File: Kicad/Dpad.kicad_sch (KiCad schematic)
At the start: 12 parts

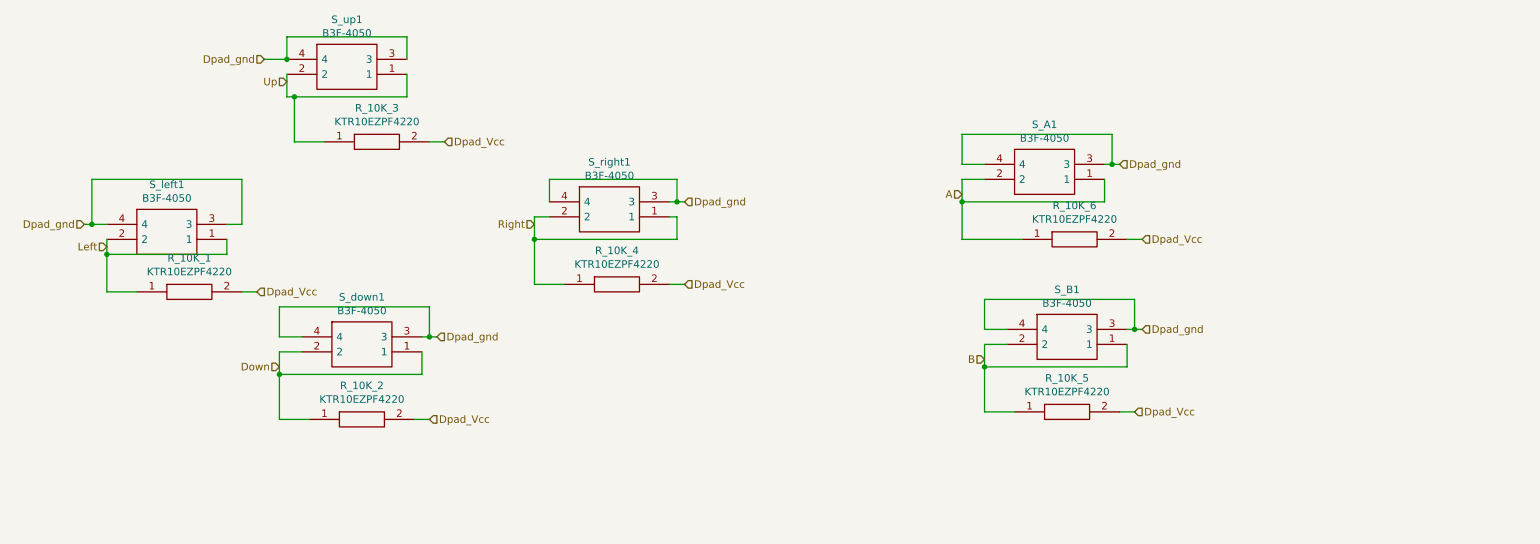
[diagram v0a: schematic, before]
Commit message: New V1.2 Hardware Release
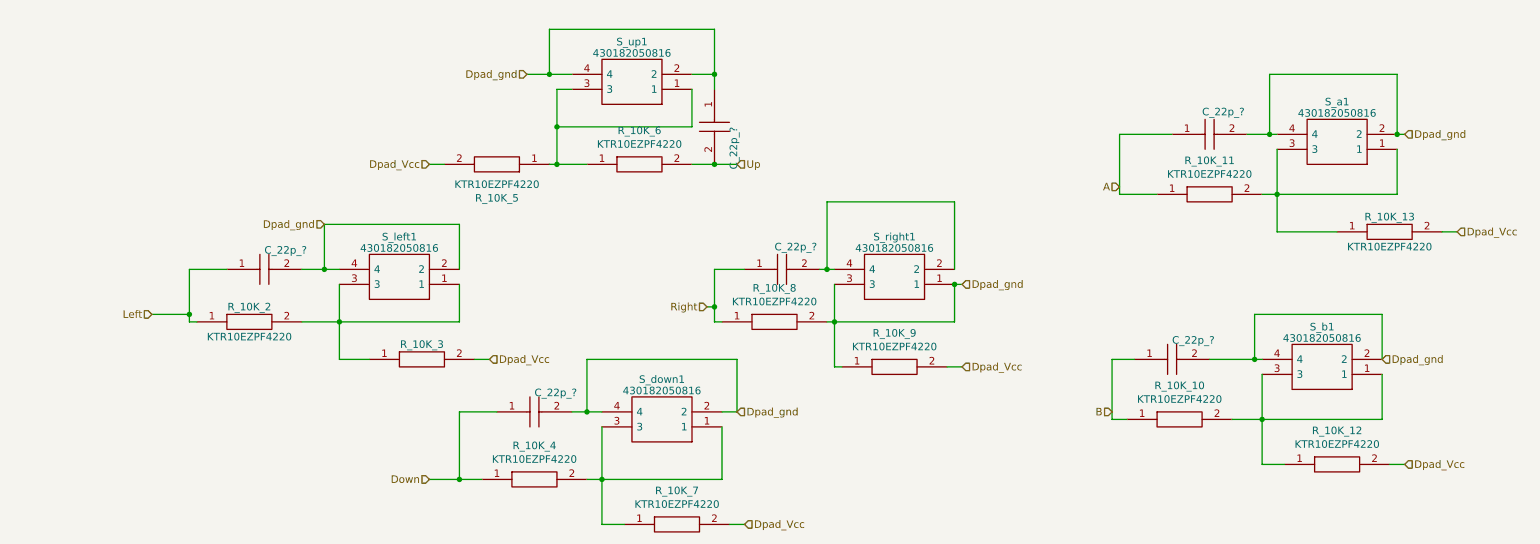
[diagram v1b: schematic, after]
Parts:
- removed S_A1, S_B1, S_down1, S_left1, S_right1, S_up1: B3F-4050, B3F-4000, symbol PicBytesMicro-rescue:B3F-4050-SamacSys_Parts
- added C_22p_? (x6): GCG21BR71H154KA01K, User_lib:CAPC2012X140N, symbol PicBytesMicro-rescue:GCG21BR71H154KA01K-SamacSys_Parts
- added R_10K_10, R_10K_11, R_10K_2, R_10K_4, R_10K_5, R_10K_8: KTR10EZPF4220, User_lib:RESC2012X75N, symbol PicBytesMicro-rescue:KTR10EZPF4220-SamacSys_Parts
- added S_a1, S_b1, S_down1, S_left1, S_right1, S_up1: 430182050816, 430182070816, symbol User_lib:430182050816
- renumbered R_10K_5 to R_10K_12, R_10K_6 to R_10K_13, R_10K_1 to R_10K_3, R_10K_3 to R_10K_6, R_10K_2 to R_10K_7, R_10K_4 to R_10K_9
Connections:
- net A: now also C_22p_?.1, R_10K_11.1; no longer R_10K_13.1
- net B: now also C_22p_?.1, R_10K_10.1; no longer R_10K_12.1
- net Down: now also C_22p_?.1, R_10K_4.1; no longer R_10K_7.1
- net Dpad_Vcc: now also R_10K_5.2; no longer R_10K_6.2
- net Dpad_gnd: now also R_10K_9.1, C_22p_?.1, C_22p_?.2, C_22p_?.2, C_22p_?.2, C_22p_?.2, R_10K_8.2, S_a1.2, S_a1.4, S_b1.2, S_b1.4, S_down1.2, S_down1.4, S_left1.2, S_left1.4, S_right1.1, S_right1.3, S_up1.2, S_up1.4
- net Left: now also C_22p_?.1, R_10K_2.1; no longer R_10K_3.1
- net Right: now also C_22p_?.1, R_10K_8.1; no longer R_10K_9.1
- net Up: now also R_10K_6.2, C_22p_?.2; no longer R_10K_6.1
- new net: R_10K_10.2, R_10K_12.1, S_b1.1, S_b1.3
- new net: R_10K_11.2, R_10K_13.1, S_a1.1, S_a1.3
- new net: R_10K_5.1, R_10K_6.1, S_up1.1, S_up1.3
- new net: R_10K_2.2, R_10K_3.1, S_left1.1, S_left1.3
- new net: R_10K_4.2, R_10K_7.1, S_down1.1, S_down1.3
- new net: C_22p_?.2, S_right1.2, S_right1.4
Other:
- company: (none) -> Making Devices
- title: (none) -> Dpad with debouncing filter
- moved on the sheet: R_10K_12, R_10K_13, R_10K_3, R_10K_6, R_10K_7, R_10K_9

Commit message: V1.25 FW release
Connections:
- net Dpad_gnd: now also C_22p_?.2, S_right1.2, S_right1.4; no longer R_10K_8.2, R_10K_9.1, S_right1.1, S_right1.3
- new net: R_10K_8.2, R_10K_9.1, S_right1.1, S_right1.3
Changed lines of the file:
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@@
   (junction (at 224.79 53.34) (diameter 0) (color 0 0 0 0)
   )
-  (junction (at 171.45 78.74) (diameter 0) (color 0 0 0 0)
-  )
   (junction (at 149.86 76.2) (diameter 0) (color 0 0 0 0)
   )
@@
   (junction (at 130.81 82.55) (diameter 0) (color 0 0 0 0)
   )
+  (junction (at 171.45 76.2) (diameter 0) (color 0 0 0 0)
+  )
   (junction (at 111.76 111.76) (diameter 0) (color 0 0 0 0)
   )
@@
     (stroke (width 0) (type default))
   )
-  (wire (pts (xy 171.45 76.2) (xy 171.45 64.77))
-    (stroke (width 0) (type default))
-  )
   (wire (pts (xy 129.54 82.55) (xy 130.81 82.55))
     (stroke (width 0) (type default))
@@
     (stroke (width 0) (type default))
   )
+  (wire (pts (xy 171.45 76.2) (xy 172.72 76.2))
+    (stroke (width 0) (type default))
+  )
   (wire (pts (xy 218.44 101.6) (xy 223.52 101.6))
     (stroke (width 0) (type default))
@@
     (stroke (width 0) (type default))
   )
+  (wire (pts (xy 171.45 64.77) (xy 171.45 76.2))
+    (stroke (width 0) (type default))
+  )
   (wire (pts (xy 226.06 69.85) (xy 226.06 63.5))
     (stroke (width 0) (type default))
@@
   )
   (wire (pts (xy 205.74 63.5) (xy 199.39 63.5))
-    (stroke (width 0) (type default))
-  )
-  (wire (pts (xy 171.45 78.74) (xy 172.72 78.74))
     (stroke (width 0) (type default))
   )
@@
     (effects (font (size 1.27 1.27)) (justify left))
   )
-  (hierarchical_label "Dpad_gnd" (shape input) (at 172.72 78.74 0) (fields_autoplaced)
+  (hierarchical_label "Dpad_gnd" (shape input) (at 172.72 76.2 0) (fields_autoplaced)
     (effects (font (size 1.27 1.27)) (justify left))
   )

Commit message: no message
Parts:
- gave numbers to parts that had none: 6

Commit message: Bill Of Materials
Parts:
- C10: renamed from C_22p_6; value GCG21BR71H154KA01K -> 100nF
- C11: renamed from C_22p_7; value GCG21BR71H154KA01K -> 100nF
- C6: renamed from C_22p_3; value GCG21BR71H154KA01K -> 100nF
- C7: renamed from C_22p_4; value GCG21BR71H154KA01K -> 100nF
- C8: renamed from C_100F_1; value GCG21BR71H154KA01K -> 100nF
- C9: renamed from C_22p_5; value GCG21BR71H154KA01K -> 100nF
- R46: renamed from R_10K_2; value KTR10EZPF4220 -> 10k
- R47: renamed from R_10K_3; value KTR10EZPF4220 -> 10k
- R48: renamed from R_10K_4; value KTR10EZPF4220 -> 10k
- R49: renamed from R_10K_5; value KTR10EZPF4220 -> 10k
- R50: renamed from R_10K_6; value KTR10EZPF4220 -> 10k
- R51: renamed from R_10K_7; value KTR10EZPF4220 -> 10k
- R52: renamed from R_10K_8; value KTR10EZPF4220 -> 10k
- R53: renamed from R_10K_9; value KTR10EZPF4220 -> 10k
- R54: renamed from R_10K_10; value KTR10EZPF4220 -> 10k
- R55: renamed from R_10K_11; value KTR10EZPF4220 -> 10k
- R56: renamed from R_10K_12; value KTR10EZPF4220 -> 10k
- R57: renamed from R_10K_13; value KTR10EZPF4220 -> 10k
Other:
- moved on the sheet: C6
